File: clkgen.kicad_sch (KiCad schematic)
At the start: 6 parts, among them U6 MS5351M

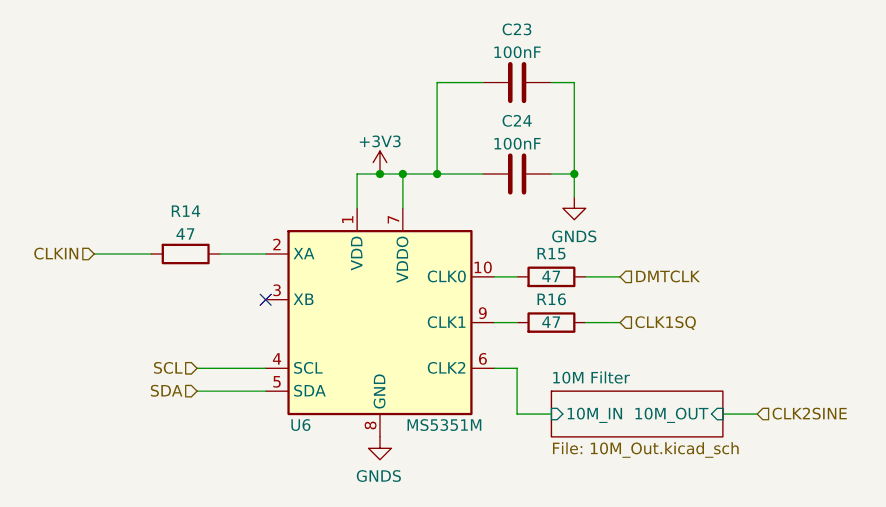
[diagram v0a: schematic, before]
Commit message: Fix 10M output filter
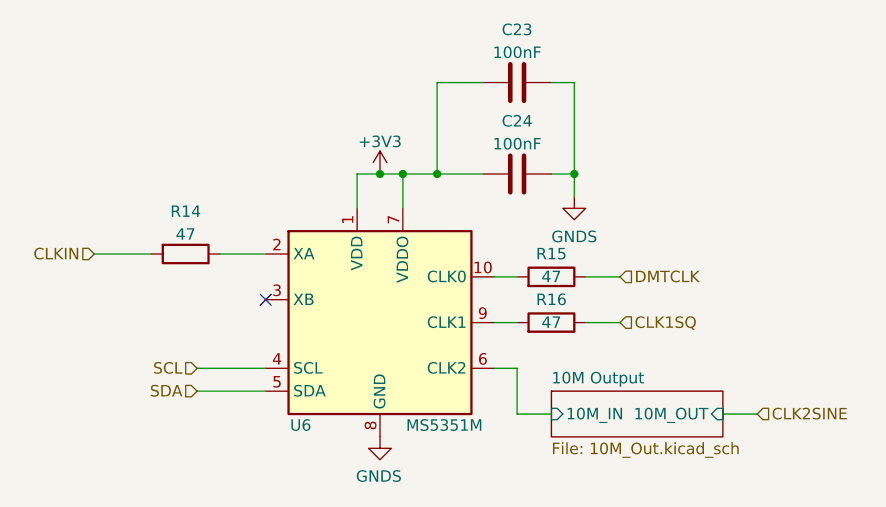
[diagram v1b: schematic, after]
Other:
- sheet 10M Filter renamed 10M Output
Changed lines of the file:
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@@
   (title_block
     (title "UCCM+BBB Carrier")
-    (date "2022-10-07")
-    (rev "1")
+    (date "2023-02-05")
+    (rev "2")
     (company "VE7XEN")
   )
@@
     (stroke (width 0.1524) (type solid) (color 0 0 0 0))
     (fill (color 255 255 194 1.0000))
-    (property "Sheet name" "10M Filter" (id 0) (at 140.97 94.5384 0)
+    (property "Sheet name" "10M Output" (id 0) (at 140.97 94.5384 0)
       (effects (font (size 1.27 1.27)) (justify left bottom))
     )
